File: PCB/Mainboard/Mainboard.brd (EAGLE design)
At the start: 60 x 150 mm, 17 parts

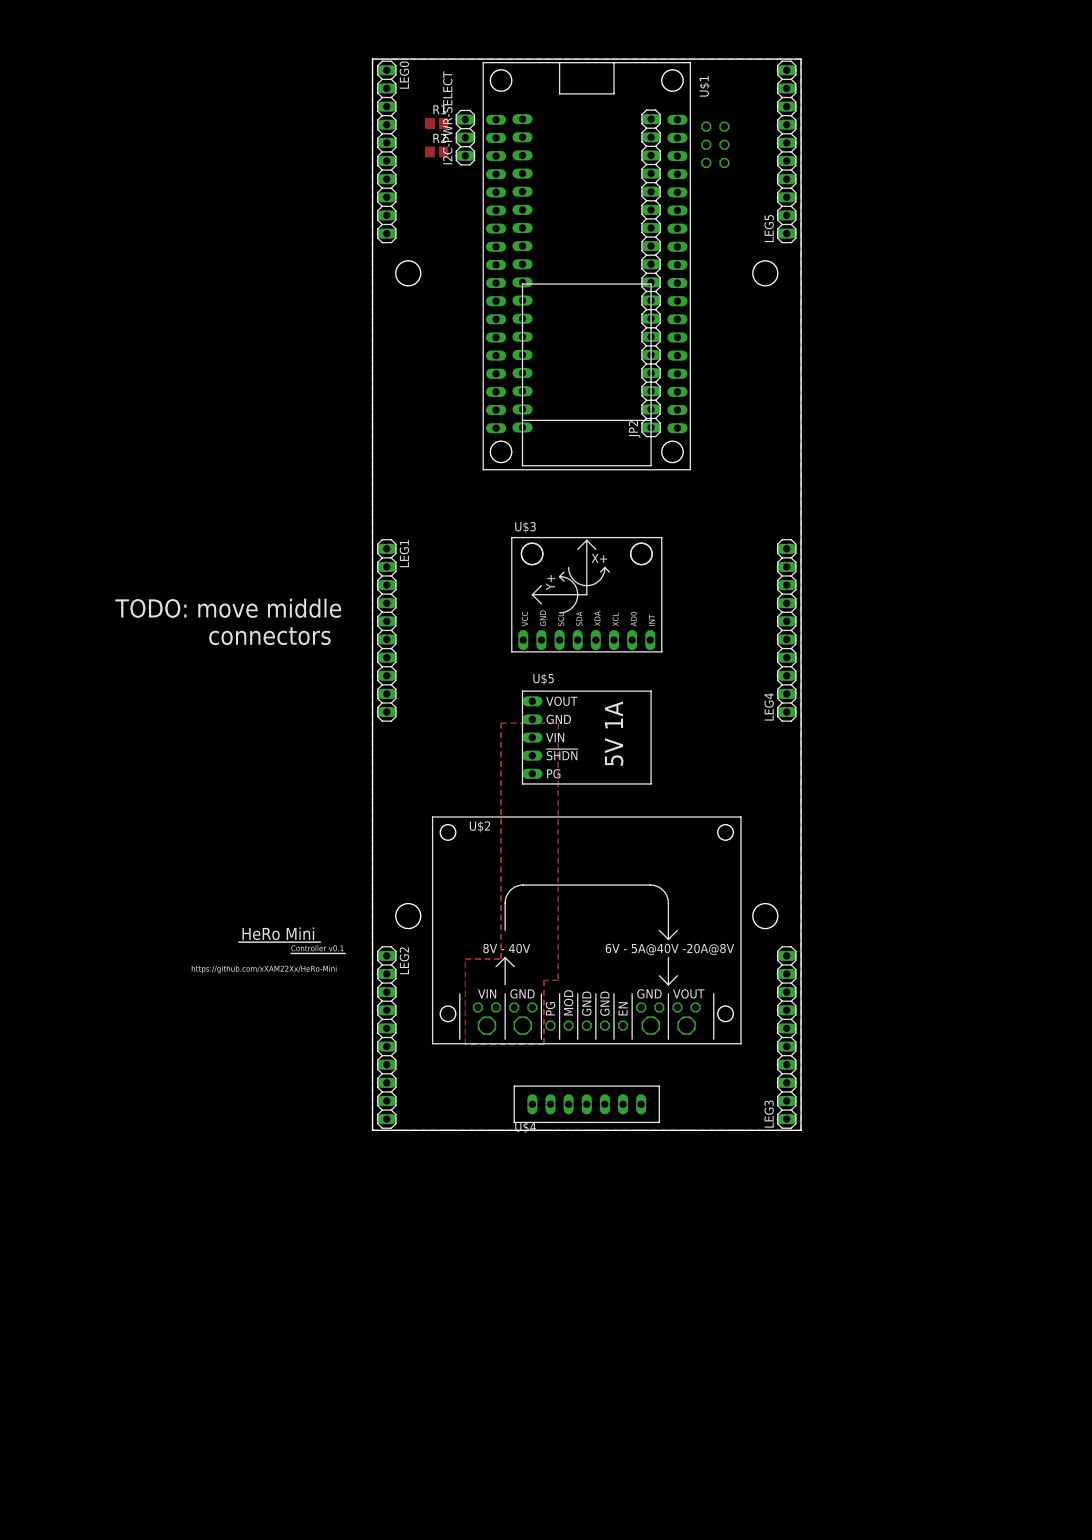
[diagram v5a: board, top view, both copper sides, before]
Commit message: Minor Redesign
Replace ESP32 Eval board with own design
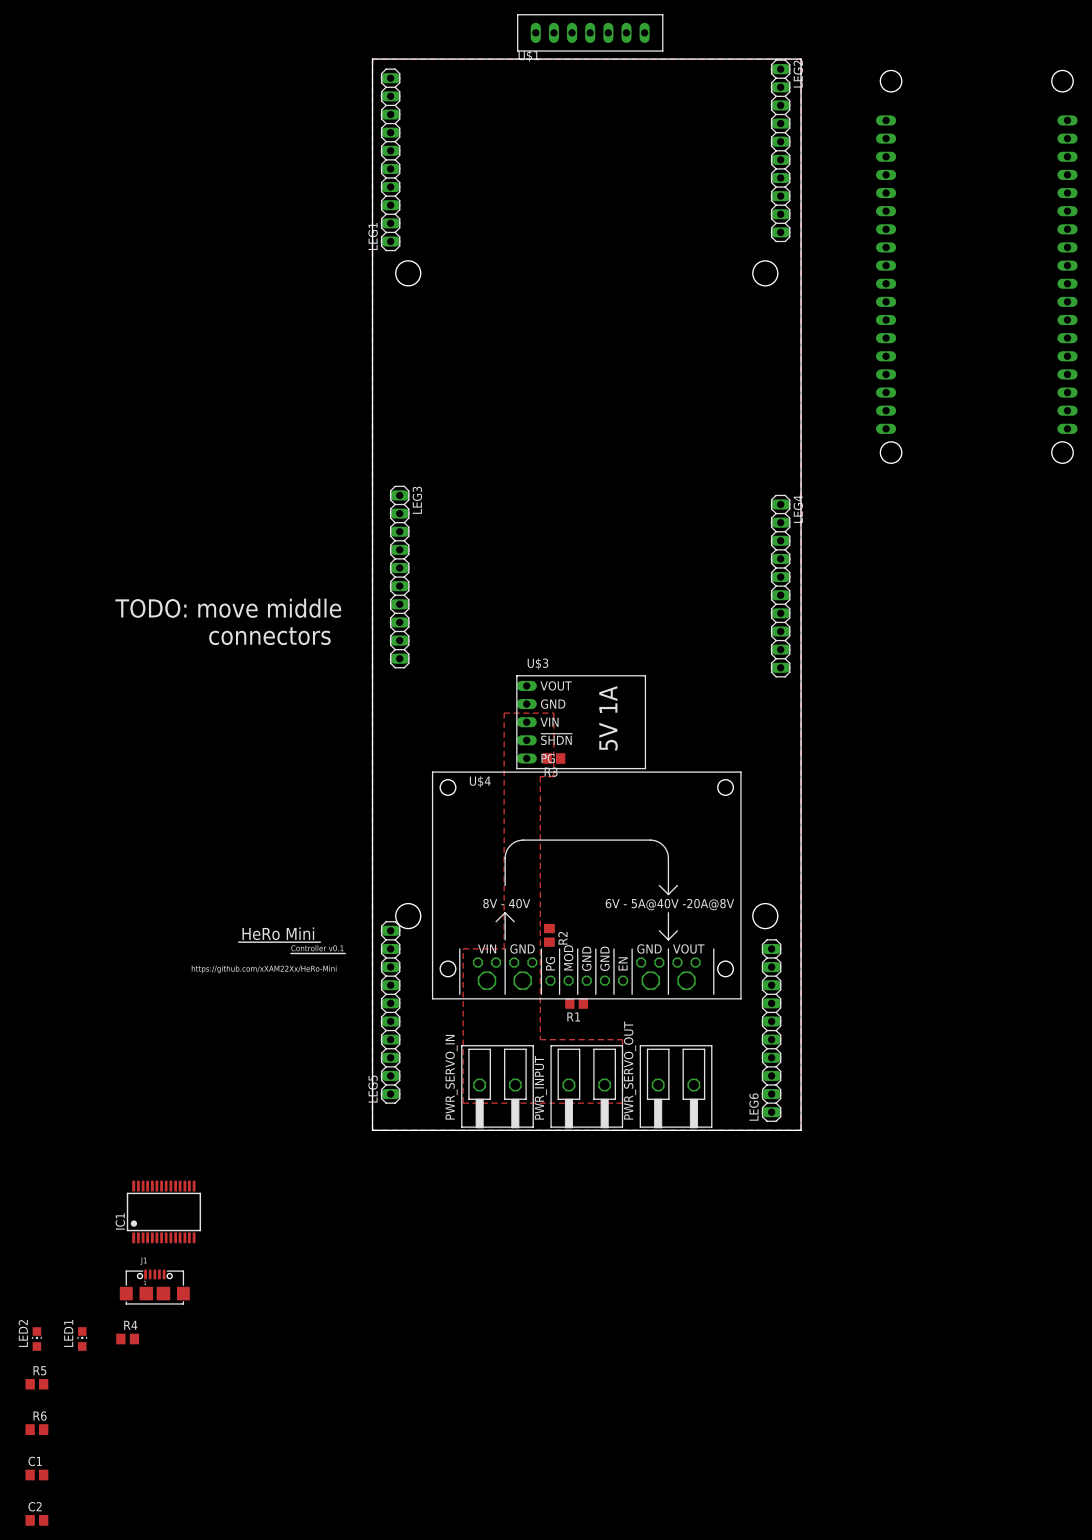
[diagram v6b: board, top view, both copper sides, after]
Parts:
- removed I2C-PWR-SELECT: (no value), pinhead:1X03
- removed JP1, JP2: (no value), pinhead:1X18
- removed LEG0: (no value), pinhead:1X10
- removed PWR-SELECT: (no value), pinhead:2X03
- removed U$2: D24V150F6, HeRo:D24V150F6
- removed U$5: D24V10F5, HeRo:D24V10F5
- added C1, C2: 100nF, rcl:C0805
- added IC1: FT232RL, ftdichip:SSOP28
- added J1: (no value), InputOutputIO (rev18a):629105136821
- added LED1, LED2: (no value), led:CHIP-LED0805
- added LEG6: (no value), pinhead:1X10
- added PWR_INPUT, PWR_SERVO_IN, PWR_SERVO_OUT: CON-PHOENIX-1935310, HeRo:CON-PHOENIX-1935310
- added R3, R4: 10k, rcl:R0805
- added R5, R6: (no value), rcl:R0805
- added U$100: ESP32-DOITV1, HeRo:ESP32-DOITV1
- U$1: value ESP32-DOITV1 -> VL53L0XV; device HeRo:ESP32-DOITV1 -> HeRo:VL53L0X_V
- U$3: value GY-521_MPU6050 -> D24V10F5; device HeRo:GY-521_MPU6050 -> HeRo:D24V10F5
- U$4: value VL53L0XV -> D24V150F6; device HeRo:VL53L0X_V -> HeRo:D24V150F6
- moved LEG2 135.9 mm to (57.1, 137.2)
- moved LEG5 132.6 mm to (2.54, 16.5)
- moved R1 124.8 mm to (28.6, 17.8), turned to 180 degrees
- moved R2 110.8 mm to (24.8, 27.3), turned to 270 degrees
- moved LEG3 84.2 mm to (3.81, 77.5), turned to 270 degrees
- moved LEG1 65.9 mm to (2.54, 135.9), turned to 90 degrees
- moved U$1 39.0 mm to (30.5, 160.0), turned to 0 degrees
- moved U$4 24.3 mm to (30.0, 34.3)
- moved U$3 17.9 mm to (29.2, 57.1), turned to 270 degrees
- moved LEG4 6.26 mm to (57.1, 76.2), turned to 270 degrees
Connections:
- removed net 3V3-1: I2C-PWR-SELECT.1, JP1.15, U$1.22
- removed net 3V3-2: I2C-PWR-SELECT.3, JP1.18, U$1.19
- removed net GND1: JP2.14, PWR-SELECT.2, U$1.5
- removed net GND2: JP2.17, PWR-SELECT.6, U$1.2
- removed net N$10: JP2.9, U$1.10
- removed net N$11: JP2.10, U$1.9
- removed net N$12: JP2.11, U$1.8
- removed net N$13: JP2.12, U$1.7
- removed net N$14: JP2.13, U$1.6
- removed net N$15: JP2.16, U$1.3
- removed net N$16: JP1.17, U$1.20
- removed net N$17: JP1.16, U$1.21
- removed net N$18: JP1.14, U$1.23
- removed net N$19: JP1.13, U$1.24
- removed net N$20: JP1.12, U$1.25
- removed net N$21: JP1.11, U$1.26
- removed net N$22: JP1.10, U$1.27
- removed net N$23: JP1.9, U$1.28
- removed net N$24: JP1.8, U$1.29
- removed net N$25: JP1.7, U$1.30
- removed net N$26: JP1.6, U$1.31
- removed net N$27: JP1.4, U$1.33
- removed net N$28: JP1.3, U$1.34
- removed net N$29: JP1.1, U$1.36
- removed net N$8: JP2.7, U$1.12
- removed net N$9: JP2.8, U$1.11
- removed net VCC1: JP2.15, PWR-SELECT.1, U$1.4
- removed net VCC2: JP2.18, PWR-SELECT.5, U$1.1
- new net !CTS: IC1.11
- new net !DTR: IC1.2
- new net !RTS: IC1.3
- new net +12V: PWR_INPUT.1, PWR_SERVO_IN.1, U$3.VIN, U$4.P$1, U$4.P$17, U$4.P$2
- new net +3V3: R2.1, R3.1
- new net EN_5V: U$3.!SHDN
- new net EN_SERVO: U$4.P$9
- new net PG_LEG: R3.2, U$3.PG
- new net PG_SERVO: R2.2, U$4.P$5
- new net RXD: IC1.5
- new net SCL_5V: U$1.SCL
- new net SDA_5V: U$1.SDA
- new net TXD: IC1.1
- new net USB_D_N: IC1.16, J1.2
- new net USB_D_P: IC1.15, J1.3
- new net VBUS: C2.1, IC1.20, J1.1
- net +5V: now also LEG6.4, U$1.VIN, U$3.VOUT; no longer LEG0.4, PWR-SELECT.3
- net GND: now also C1.2, C2.2, IC1.18, IC1.21, IC1.25, IC1.26, IC1.7, J1.5, LEG6.10, LEG6.8, LEG6.9, PWR_INPUT.2, PWR_SERVO_IN.2, PWR_SERVO_OUT.1, R1.1, U$1.GND, U$3.GND, U$4.P$10, U$4.P$11, U$4.P$14, U$4.P$16, U$4.P$3, U$4.P$4, U$4.P$7, U$4.P$8; no longer LEG0.10, LEG0.8, LEG0.9, PWR-SELECT.4
- net N$1: now also C1.1, IC1.17, IC1.4, R4.1, R5.2, R6.2; no longer I2C-PWR-SELECT.2, R1.2, R2.2
- net N$2: now also R1.2, U$4.P$6; no longer JP2.1, U$1.18
- net N$3: now also IC1.19, R4.2; no longer JP2.2, U$1.17
- net N$4: now also IC1.23, LED1.C; no longer JP2.3, U$1.16
- net N$5: now also IC1.22, LED2.C; no longer JP2.4, U$1.15
- net N$6: now also LED1.A, R5.1; no longer JP2.5, U$1.14
- net N$7: now also LED2.A, R6.1; no longer JP2.6, U$1.13
- net SCL: now also LEG6.5; no longer JP1.2, LEG0.5, R2.1, U$1.35
- net SDA: now also LEG6.6; no longer JP1.5, LEG0.6, R1.1, U$1.32
- net VDD: now also LEG6.1, LEG6.2, LEG6.3, PWR_SERVO_OUT.2, U$4.P$12, U$4.P$13, U$4.P$15; no longer LEG0.1, LEG0.2, LEG0.3
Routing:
- added copper zone on layer 1, net +12V
- removed copper zone on layer 1, net +5V

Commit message: added new parts, added all signals
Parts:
- removed U$100: ESP32-DOITV1, HeRo:ESP32-DOITV1
- added C3: 100nF, rcl:C0805
- added C4, C5, C6: 1nF, rcl:C0805
- added LED3, LED4, LED5, LED6, LED7: (no value), led:CHIP-LED0805
- added R10, R12, R9: 1k, rcl:R0805
- added R11, R22, R23, R24, R25, R7, R8: 10k, rcl:R0805
- added R13, R14: 470R, rcl:R0805
- added R15, R16, R17, R18, R21: (no value), rcl:R0805
- added R19, R20, R27, R28: 0R, rcl:R0805
- added R26: 200k, rcl:R0805
- added S1, S2: (no value), switch-omron:B3F-10XX
- added S3, S4, S5: (no value), switch:255SB
- added SJ1: (no value), jumper:SJ
- added T1, T2: BC847, transistor:SOT23
- added U$2: ESP32-WROOM-32U, HeRo:ESP32-WROOM-32U
- added U$5: BLUEDOT-BNO055, HeRo:BLUEDOT-BNO055
- added U$6: D24V10F3, HeRo:D24V10F5
- added U$7: PCA9306, HeRo:PCA9306
- moved C2 211.6 mm to (27.3, 143.6), flipped to the bottom
- moved R6 211.4 mm to (46.1, 147.9), flipped to the bottom, turned to 180 degrees
- moved C1 210.6 mm to (46.8, 140.2), flipped to the bottom, turned to 90 degrees
- moved R5 203.7 mm to (46.1, 145.6), flipped to the bottom, turned to 180 degrees
- moved LED2 198.2 mm to (42.3, 147.7), flipped to the bottom, turned to 270 degrees
- moved LED1 193.7 mm to (42.3, 145.8), flipped to the bottom, turned to 270 degrees
- moved R4 190.5 mm to (38.1, 147.0), flipped to the bottom, turned to 270 degrees
- moved J1 181.8 mm to (30.0, 148.6), flipped to the bottom, turned to 180 degrees
- moved IC1 166.5 mm to (39.8, 140.1), flipped to the bottom
- moved U$1 28.0 mm to (31.8, 188.0)
- moved R3 13.5 mm to (35.6, 61.0)
- moved U$3 8.98 mm to (20.3, 58.4), turned to 90 degrees
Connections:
- removed net N$1: C1.1, IC1.17, IC1.4, R4.1, R5.2, R6.2
- removed net SCL: LEG1.5, LEG2.5, LEG3.5, LEG4.5, LEG5.5, LEG6.5
- removed net SDA: LEG1.6, LEG2.6, LEG3.6, LEG4.6, LEG5.6, LEG6.6
- new net CLK: U$2.20
- new net CMD: U$2.19
- new net EN: C4.1, R11.1, R13.1, T1.3, U$2.3
- new net EN_3V3: S5.2, U$6.!SHDN
- new net IMU_ADR: SJ1.1, U$5.ADR
- new net IMU_INT: R21.1, U$5.INT
- new net IO0: R14.1, T2.3, U$2.25
- new net IO12: U$2.14
- new net IO13: U$2.16
- new net IO14: U$2.13
- new net IO15: U$2.23
- new net IO16: U$2.27
- new net IO17: R21.2, U$2.28
- new net IO18: R19.1, U$2.30
- new net IO19: R20.1, U$2.31
- new net IO2: R12.2, U$2.24
- new net IO21: U$2.33
- new net IO22: R27.1, U$2.36
- new net IO23: R28.1, U$2.37
- new net IO25: U$2.10
- new net IO26: U$2.11
- new net IO27: U$2.12
- new net IO32: U$2.8
- new net IO33: U$2.9
- new net IO34: U$2.6
- new net IO35: U$2.7
- new net IO4: U$2.26
- new net IO5: U$2.29
- new net N$12: LED3.A, R12.1
- new net N$13: C5.1, R13.2, S1.1, S1.2
- new net N$14: C6.1, R14.2, S2.1, S2.2
- new net N$15: LED5.A, R16.1
- new net N$16: LED6.A, R17.1
- new net N$17: LED4.A, R15.1
- new net N$18: LED7.A, R18.1
- new net N$23: R26.2, U$7.EN, U$7.VREF2
- new net N$8: R7.1, T1.1
- new net N$9: R8.1, T2.1
- new net RXD0: R9.2, U$2.34
- new net SCL_3V3: R22.2, R27.2, U$7.SCL1
- new net SD0: U$2.21
- new net SD1: U$2.22
- new net SD2: U$2.17
- new net SD3: U$2.18
- new net SDA_3V3: R23.2, R28.2, U$7.SDA1
- new net SN: U$2.5
- new net SP: U$2.4
- new net TXD0: R10.2, U$2.35
- net !DTR: now also R7.2, T2.2
- net !RTS: now also R8.2, T1.2
- net +12V: now also R18.2, U$6.VIN
- net +3V3: now also C1.1, C3.1, IC1.4, R11.2, R15.2, R22.1, R23.1, R4.1, R5.2, R6.2, U$2.2, U$6.VOUT, U$7.VREF1
- net +5V: now also R16.2, R24.1, R25.1, R26.1, U$5.VCC
- net EN_5V: now also S4.2
- net EN_SERVO: now also S3.2
- net GND: now also C3.2, C4.2, C5.2, C6.2, LED3.C, LED4.C, LED5.C, LED6.C, LED7.C, S1.3, S1.4, S2.3, S2.4, S3.3, S4.3, S5.3, SJ1.2, U$2.1, U$2.15, U$2.38, U$2.39, U$5.GND, U$6.GND, U$7.GND
- net PG_LEG: now also R19.2
- net PG_SERVO: now also R20.2
- net RXD: now also R10.1
- net SCL_5V: now also LEG1.5, LEG2.5, LEG3.5, LEG4.5, LEG5.5, LEG6.5, R24.2, U$5.SCL, U$7.SCL2
- net SDA_5V: now also LEG1.6, LEG2.6, LEG3.6, LEG4.6, LEG5.6, LEG6.6, R25.2, U$5.SDA, U$7.SDA2
- net TXD: now also R9.1
- net VDD: now also R17.2
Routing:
- added copper zone on layer 1, net +3V3

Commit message: minor adjustments, finished routing
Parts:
- removed R19, R20: 0R, rcl:R0805
- removed R2, R3: 10k, rcl:R0805
- removed R21: (no value), rcl:R0805
- removed S1, S2: (no value), switch-omron:B3F-10XX
- removed U$1: VL53L0XV, HeRo:VL53L0X_V
- added U$8, U$9: TASTER9313, HeRo:TASTER9313
- moved S5 97.5 mm to (30.5, 117.2), flipped to the bottom, turned to 180 degrees
- moved S4 87.0 mm to (30.5, 109.9), flipped to the bottom, turned to 180 degrees
- moved LED4 82.9 mm to (17.2, 130.4), flipped to the bottom
- moved R15 79.3 mm to (17.2, 128.3), flipped to the bottom, turned to 180 degrees
- moved S3 76.1 mm to (30.5, 102.1), flipped to the bottom, turned to 180 degrees
- moved R17 75.2 mm to (45.0, 10.6), flipped to the bottom, turned to 270 degrees
- moved LED6 74.3 mm to (40.0, 10.5), flipped to the bottom, turned to 180 degrees
- moved C6 71.0 mm to (26.2, 135.0), flipped to the bottom
- moved R28 68.1 mm to (42.2, 147.4)
- moved R14 67.7 mm to (28.3, 135.0), flipped to the bottom
- moved C5 66.7 mm to (17.3, 148.0), flipped to the bottom, turned to 180 degrees
- moved R23 66.6 mm to (46.2, 147.4), turned to 180 degrees
- moved R13 65.4 mm to (17.3, 145.4), flipped to the bottom, turned to 0 degrees
- moved R22 63.4 mm to (46.2, 145.3), turned to 180 degrees
- moved R27 63.2 mm to (42.2, 145.3)
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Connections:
- removed net PG_LEG: R19.2, R3.2, U$3.PG
- removed net PG_SERVO: R2.2, R20.2, U$4.P$5
- net +3V3: no longer R2.1, R3.1
- net +5V: no longer U$1.VIN
- net GND: now also U$8.1, U$8.2, U$9.1, U$9.2; no longer S1.3, S1.4, S2.3, S2.4, U$1.GND
- net IMU_INT: no longer R21.1
- net IO17: no longer R21.2
- net IO18: no longer R19.1
- net IO19: no longer R20.1
- net N$13: now also U$8.3; no longer S1.1, S1.2
- net N$14: now also U$9.4; no longer S2.1, S2.2
- net SCL_5V: no longer U$1.SCL
- net SDA_5V: no longer U$1.SDA
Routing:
- net SCL_5V: track 0.00 -> 391.5 mm, vias 0 -> 7
- net SDA_5V: track 0.00 -> 387.8 mm, vias 0 -> 6
- net EN_SERVO: track 0.00 -> 88.6 mm, vias 0 -> 2
- net EN_5V: track 0.00 -> 62.3 mm, vias 0 -> 2
- net EN_3V3: track 0.00 -> 60.1 mm, vias 0 -> 2
- net EN: track 0.00 -> 54.1 mm, vias 0 -> 1
- net IO0: track 0.00 -> 26.9 mm, vias 0 -> 1
- net TXD0: track 0.00 -> 26.7 mm, vias 0 -> 1
- net +3V3: track 0.00 -> 19.7 mm, vias 0 -> 26
- net RXD0: track 0.00 -> 19.3 mm, vias 0 -> 1
- net VBUS: track 0.00 -> 17.7 mm
- net +5V: track 0.00 -> 16.3 mm, vias 0 -> 1
- net GND: track 0.00 -> 16.2 mm, vias 0 -> 17
- net !RTS: track 0.00 -> 14.9 mm, vias 0 -> 2
- net USB_D_N: track 0.00 -> 13.3 mm
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- added copper zone on layer 16, net +3V3
- added copper zone on layer 1, net +5V
- added copper zone on layer 16, net +5V
- added copper zone on layer 1, net GND
